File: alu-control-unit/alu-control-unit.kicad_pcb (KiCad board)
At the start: 2 copper layers, 346.7 x 55.9 mm, 37 parts, among them J1 Conn_01x08, J2 Conn_01x08, J3 Conn_01x04, J4 Conn_01x01, J5 Conn_01x08, J6 Conn_01x03, J7 PWR-2_pole_power_connector, U1 8-bit-bitwise-logic, U2 4-way-8-bit-bus-selector, U3 8_bit_xor, U4 8_bit_adder, U5 4-way-8-bit-bus-selector, U6 8-input-NOR

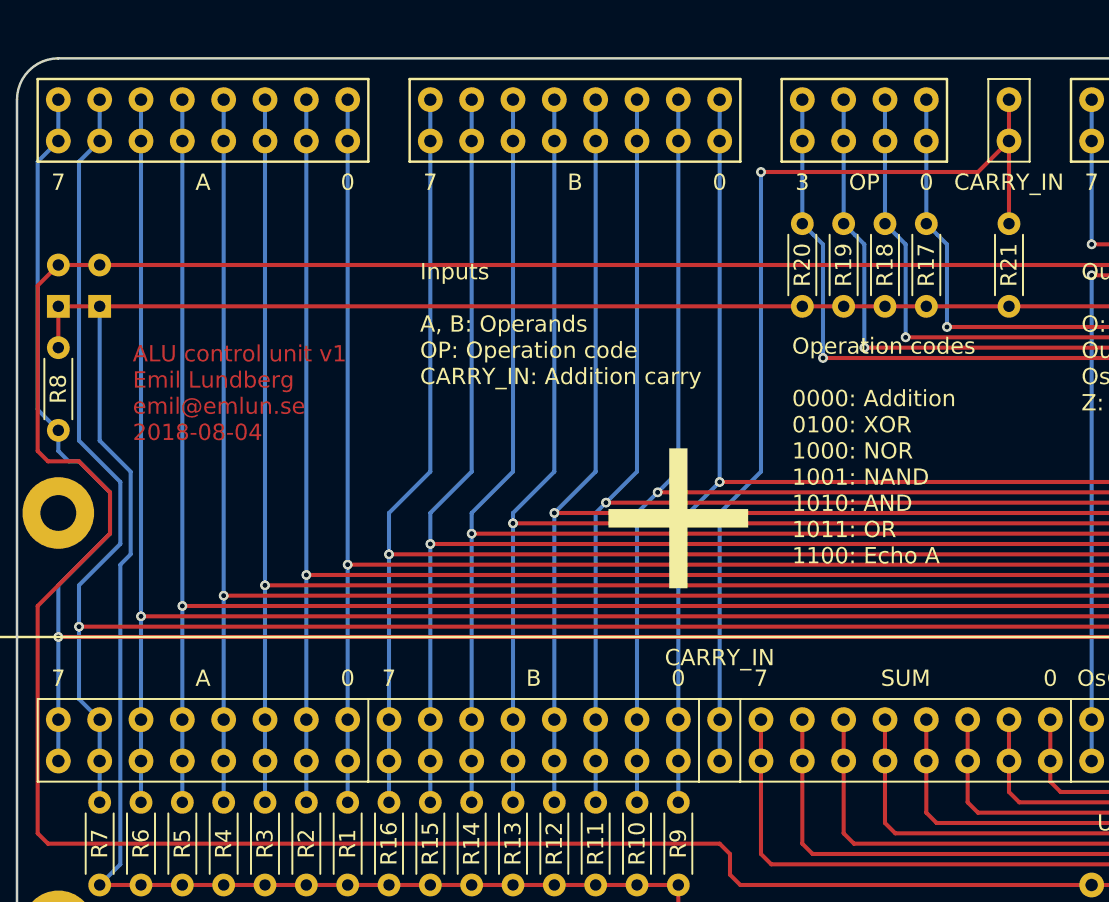
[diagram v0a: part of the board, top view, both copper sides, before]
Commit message: Make pull-down resistor connections visible on front side
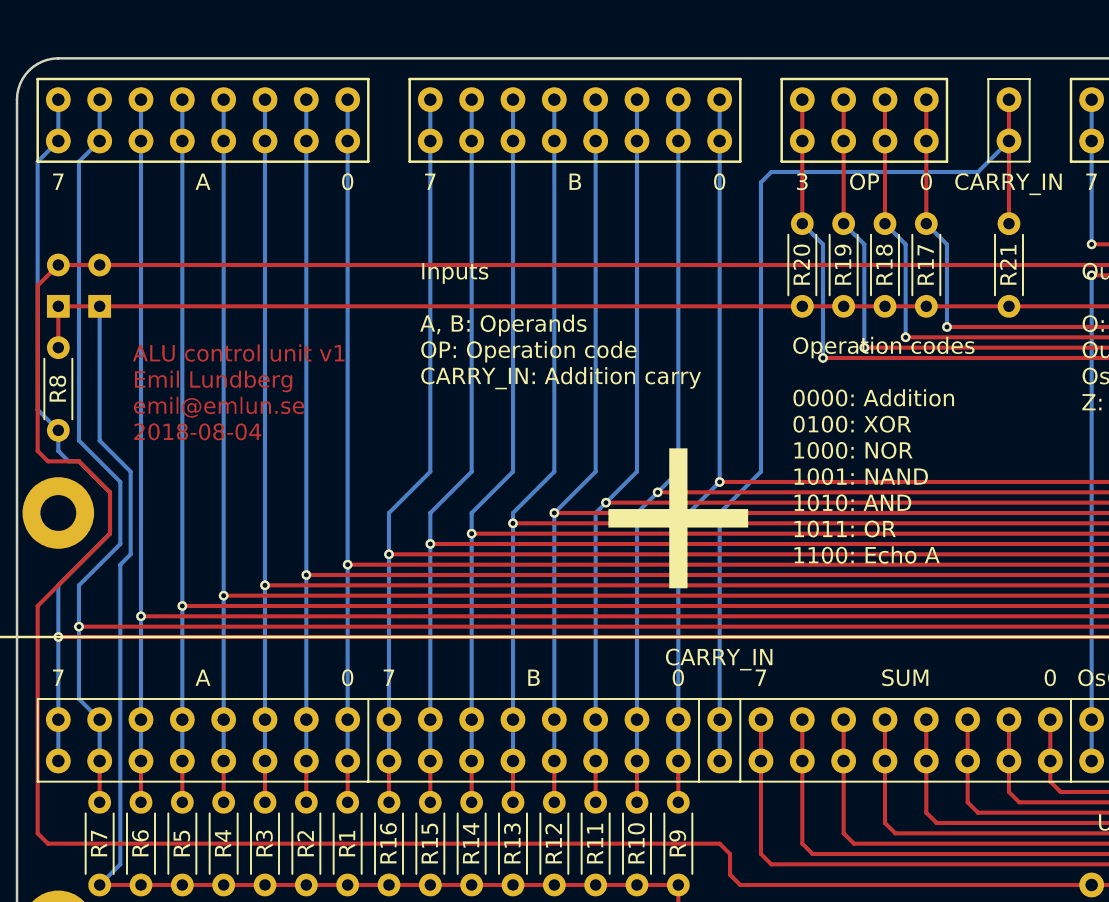
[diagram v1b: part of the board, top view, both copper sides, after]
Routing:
- net /carry_in: track 60.9 -> 60.5 mm, vias 1 -> 0

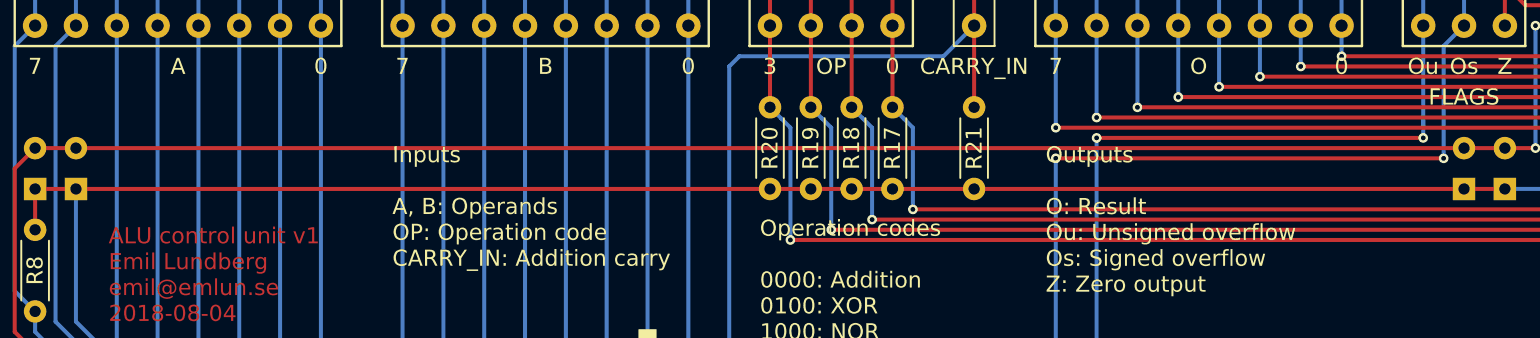
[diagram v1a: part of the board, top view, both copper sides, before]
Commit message: Add VCC and GND labels to ALU control unit PCB
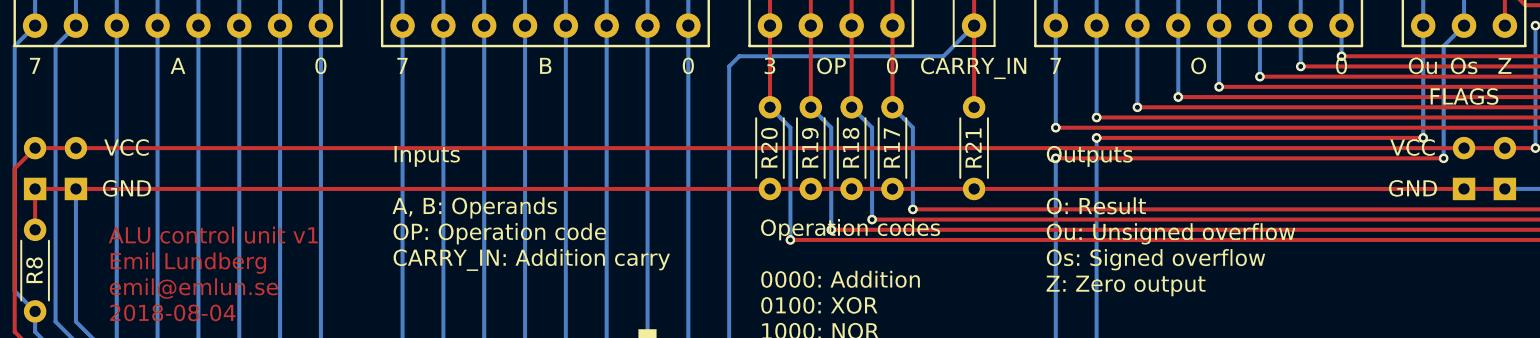
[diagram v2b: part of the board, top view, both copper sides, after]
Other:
- board text added: "GND"
- board text added: "VCC"
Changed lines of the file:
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@@
   (general
     (thickness 1.6)
-    (drawings 51)
+    (drawings 55)
     (tracks 1002)
     (zones 0)
@@
     )
   )
+  (gr_text GND (at 108.585 76.2) (layer F.SilkS)
+    (effects (font (size 1 1) (thickness 0.15)))
+  )
+  (gr_text GND (at 28.575 76.2) (layer F.SilkS)
+    (effects (font (size 1 1) (thickness 0.15)))
+  )
+  (gr_text VCC (at 108.585 73.66) (layer F.SilkS)
+    (effects (font (size 1 1) (thickness 0.15)))
+  )
+  (gr_text VCC (at 28.575 73.66) (layer F.SilkS)
+    (effects (font (size 1 1) (thickness 0.15)))
+  )
   (gr_text 0 (at 133.35 92.71) (layer F.SilkS)

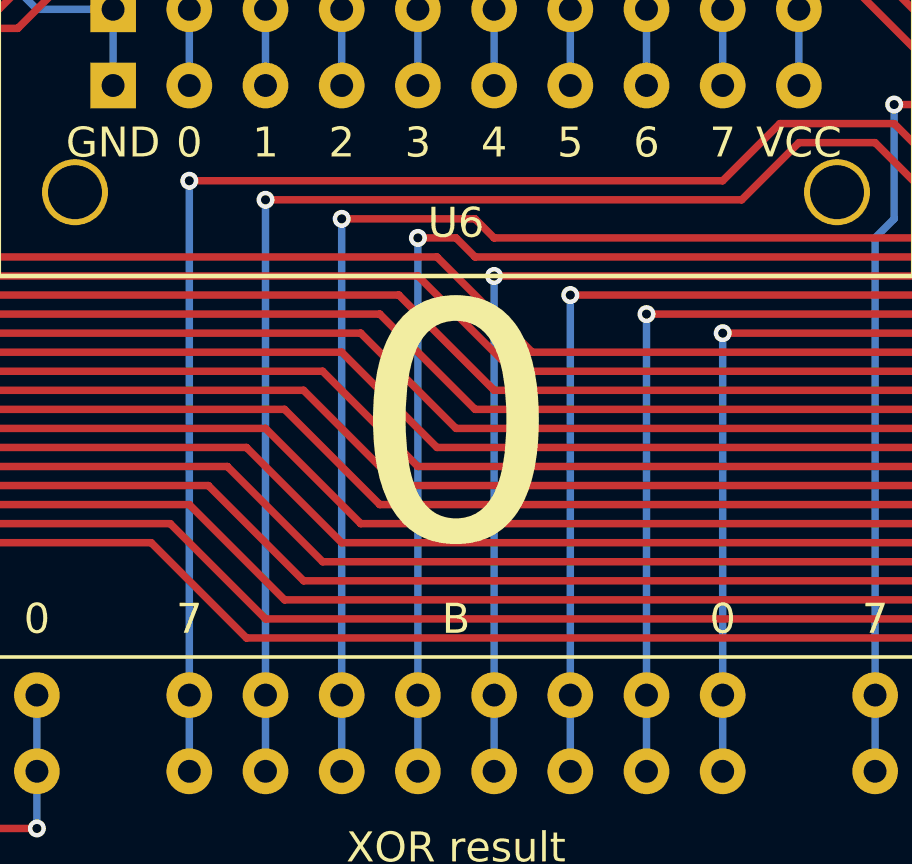
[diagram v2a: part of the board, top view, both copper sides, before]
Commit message: Add ? to zero detector subsystem label
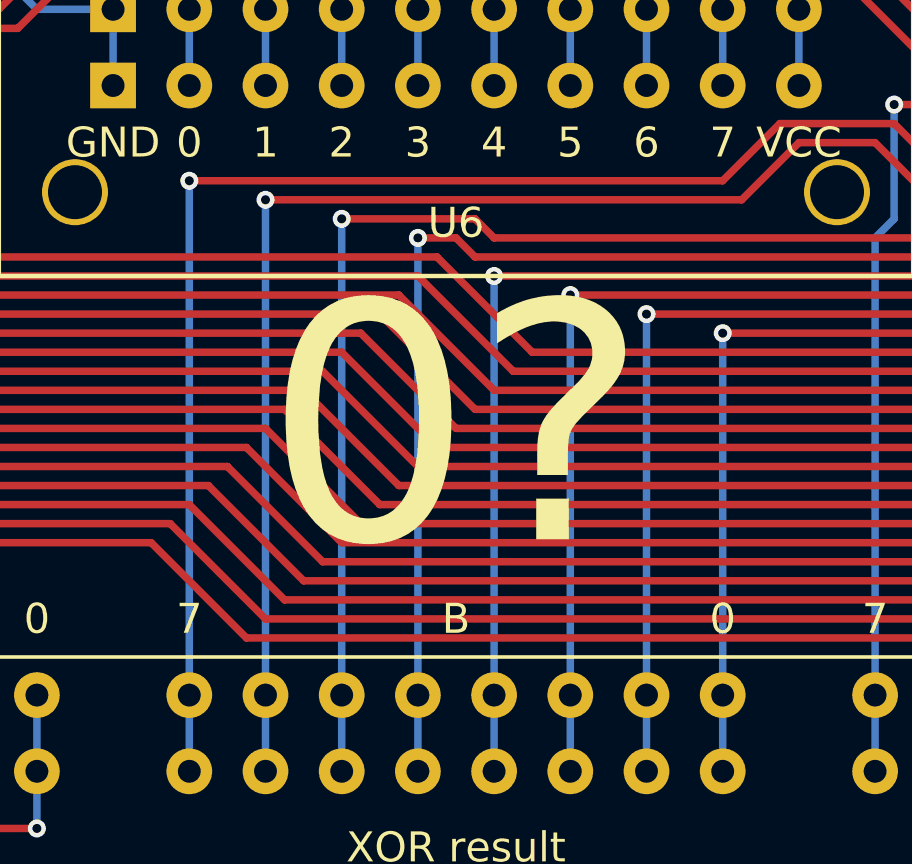
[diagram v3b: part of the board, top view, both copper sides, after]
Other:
- board text added: "0?"
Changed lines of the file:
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@@
     (effects (font (size 1 1) (thickness 0.15)))
   )
-  (gr_text 0 (at 133.35 92.71) (layer F.SilkS)
+  (gr_text 0? (at 133.35 92.71) (layer F.SilkS)
     (effects (font (size 8 8) (thickness 0.6)))
   )

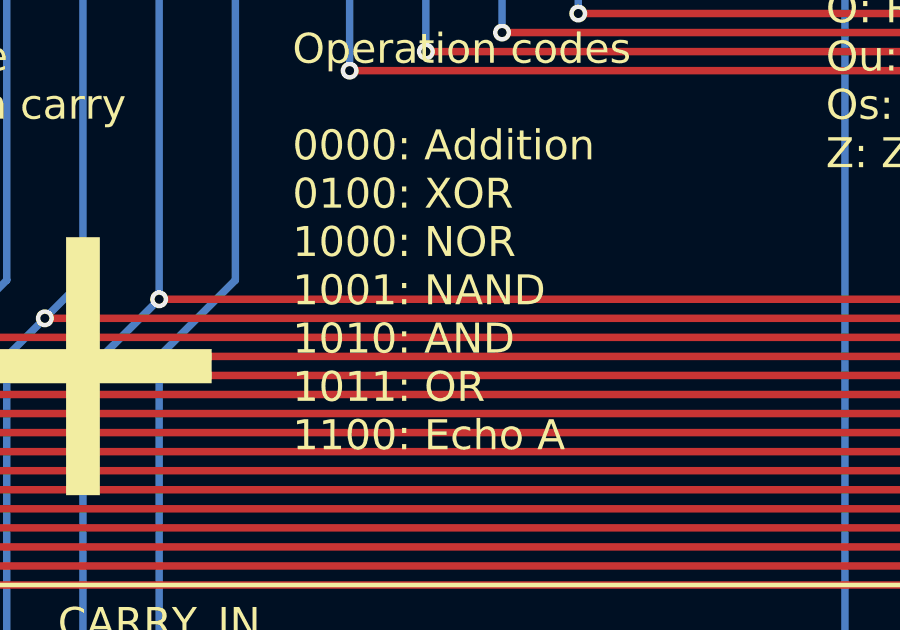
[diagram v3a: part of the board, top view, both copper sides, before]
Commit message: Fix order of boolean operations in opcodes label
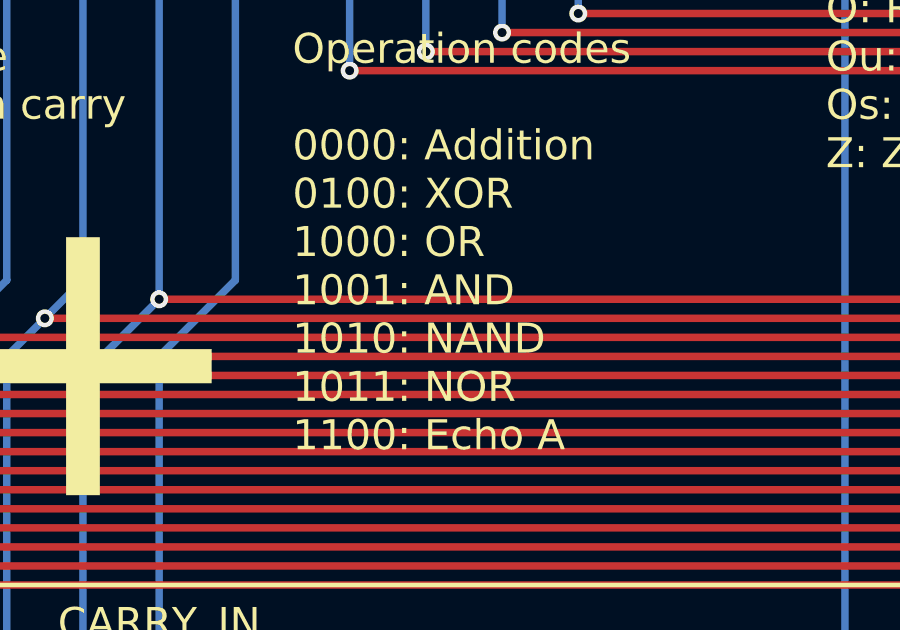
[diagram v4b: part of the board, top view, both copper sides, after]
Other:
- board text added: "Operation codes 0000: Addition 0100: XOR 1000: OR 1001: AND 1010: NAND 1011: NOR 1100: Echo A"
- board text removed: "Operation codes 0000: Addition 0100: XOR 1000: NOR 1001: NAND 1010: AND 1011: OR 1100: Echo A"
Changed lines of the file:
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@@
     (effects (font (size 8 8) (thickness 0.6)))
   )
-  (gr_text "Operation codes\n\n0000: Addition\n0100: XOR\n1000: NOR\n1001: NAND\n1010: AND\n1011: OR\n1100: Echo A" (at 67.945 85.09) (layer F.SilkS)
+  (gr_text "Operation codes\n\n0000: Addition\n0100: XOR\n1000: OR\n1001: AND\n1010: NAND\n1011: NOR\n1100: Echo A" (at 67.945 85.09) (layer F.SilkS)
     (effects (font (size 1 1) (thickness 0.12)) (justify left))
   )
